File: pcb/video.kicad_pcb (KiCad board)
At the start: 4 copper layers, 159.9 x 99.9 mm, 170 parts, among them J1 09031966921, J3 Conn_02x07_Counter_Clockwise, J7 DB15_Female_HighDensity, J8 HDMI_A, SW1 SW_Push, U1 NCP115, U10 NCA9306DPH, U11 S62LV256AL-45TLI, U12 XC9572XL-10VQG44C, U2 LP3853ESX-3.3/NOPB, U3 LCMXO2-1200HC-4TG100I, U4 LCMXO2-7000HC-4TG144C, U5 THS8136, U6 TFP410PAP, U7 ESD224DQA, U8 ESD224DQA, U9 PCA9540BDP, X1 ASV-xxxMHz

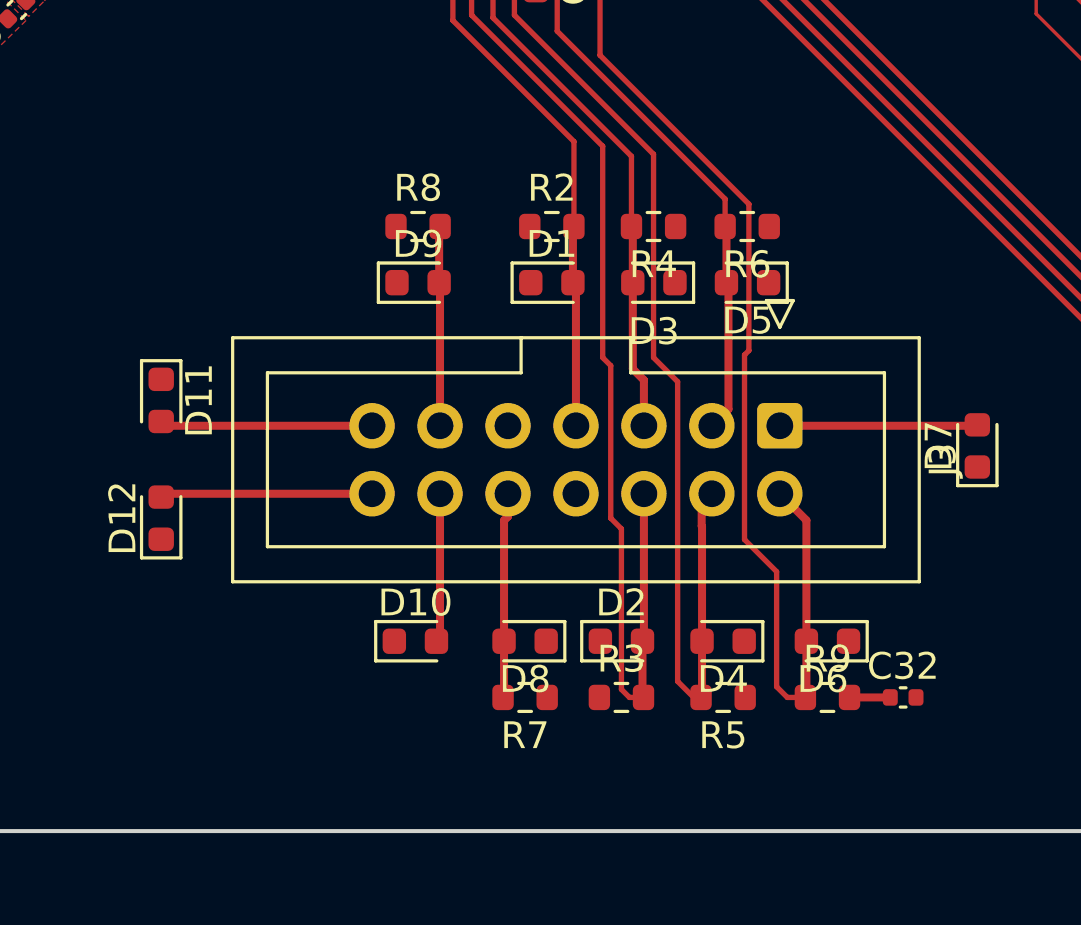
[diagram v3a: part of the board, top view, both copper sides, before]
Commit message: add the programming controller's jtag to the connector
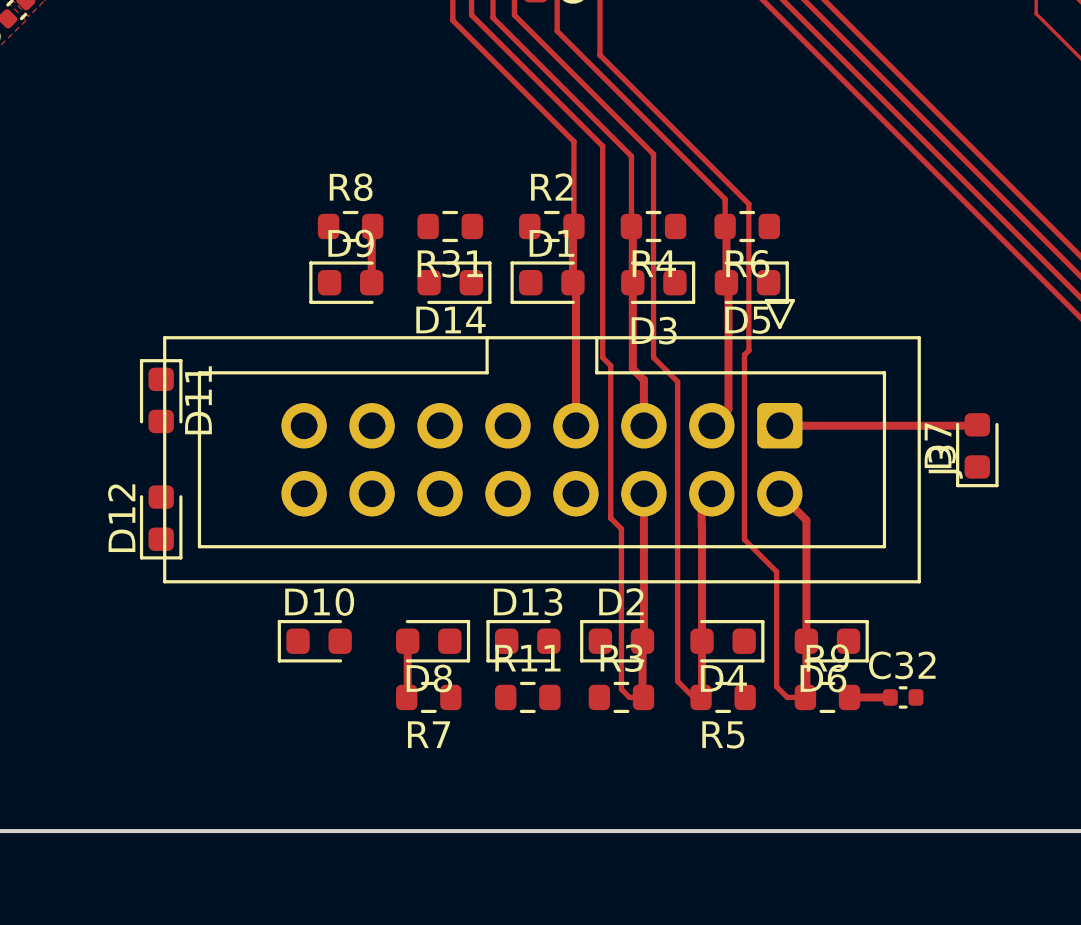
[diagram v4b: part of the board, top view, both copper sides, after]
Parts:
- added D13: D_TVS, Diode_SMD:D_0603_1608Metric, F.Cu at (152.7, 137.8)
- added D14: D_TVS, Diode_SMD:D_0603_1608Metric, F.Cu at (149.8, 124.4)
- added R11: 10k, Resistor_SMD:R_0603_1608Metric, F.Cu at (152.7, 139.9)
- added R31: 10k, Resistor_SMD:R_0603_1608Metric, F.Cu at (149.8, 122.3)
- J3: value Conn_02x07_Counter_Clockwise -> Conn_02x08_Counter_Clockwise; footprint Connector_IDC:IDC-Header_2x07_P2.54mm_Vertical -> Connector_IDC:IDC-Header_2x08_P2.54mm_Vertical
- moved D8 3.60 mm to (149.0, 137.8)
- moved R7 3.60 mm to (149.0, 139.9)
- moved D10 3.60 mm to (144.9, 137.8)
- moved D9 2.52 mm to (146.1, 124.4)
- moved R8 2.52 mm to (146.1, 122.3)
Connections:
- J3 pad 10: VIDEO_CTRL_CONFIG_SN -> GND
- J3 pad 11: BUS_CTRL_CONFIG_SN -> PROG_CTRL_TDO
- J3 pad 12: MISO -> VIDEO_CTRL_CONFIG_SN
- J3 pad 13: MOSI -> BUS_CTRL_CONFIG_SN
- J3 pad 14: CCK -> MISO
- J3 pad 8: GND -> PROG_CTRL_TDI
- U12 pad 10: (no net) -> JTAG_TMS_IN
- U12 pad 11: (no net) -> JTAG_TCK_IN
- U12 pad 24: (no net) -> PROG_CTRL_TDO
- U12 pad 9: (no net) -> PROG_CTRL_TDI
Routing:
- net CCK: track 7.93 -> 0.18 mm
- net MOSI: track 7.95 -> 0.23 mm
- net VIDEO_CTRL_CONFIG_SN: track 7.69 -> 2.12 mm
- net MISO: track 5.57 -> 0.19 mm
- net BUS_CTRL_CONFIG_SN: track 7.48 -> 2.16 mm

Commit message: add shield
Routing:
- net PROG_CTRL_TDI: track 0.00 -> 46.6 mm
- net PROG_CTRL_TDO: track 0.00 -> 41.2 mm, vias 0 -> 2
- net VIDEO_CTRL_CONFIG_SN: track 2.12 -> 28.0 mm
- net CONN_32: track 17.1 -> 0.00 mm
- net CONN_31: track 0.00 -> 17.1 mm
- net VGA_DDC_SCL: track 32.1 -> 19.4 mm
- net +5V: track 238.5 -> 230.5 mm
- net JTAG_TCK_IN: track 42.7 -> 50.4 mm
- net VGA_HSYNC: track 91.3 -> 84.6 mm
- net MISO: track 0.19 -> 6.19 mm
- net BUS_CTRL_CONFIG_SN: track 2.16 -> 7.51 mm
- net VGA_VSYNC: track 99.8 -> 94.5 mm
- net CCK: track 0.18 -> 5.39 mm
- net MOSI: track 0.23 -> 5.41 mm
- net JTAG_TMS_IN: track 27.8 -> 30.6 mm
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
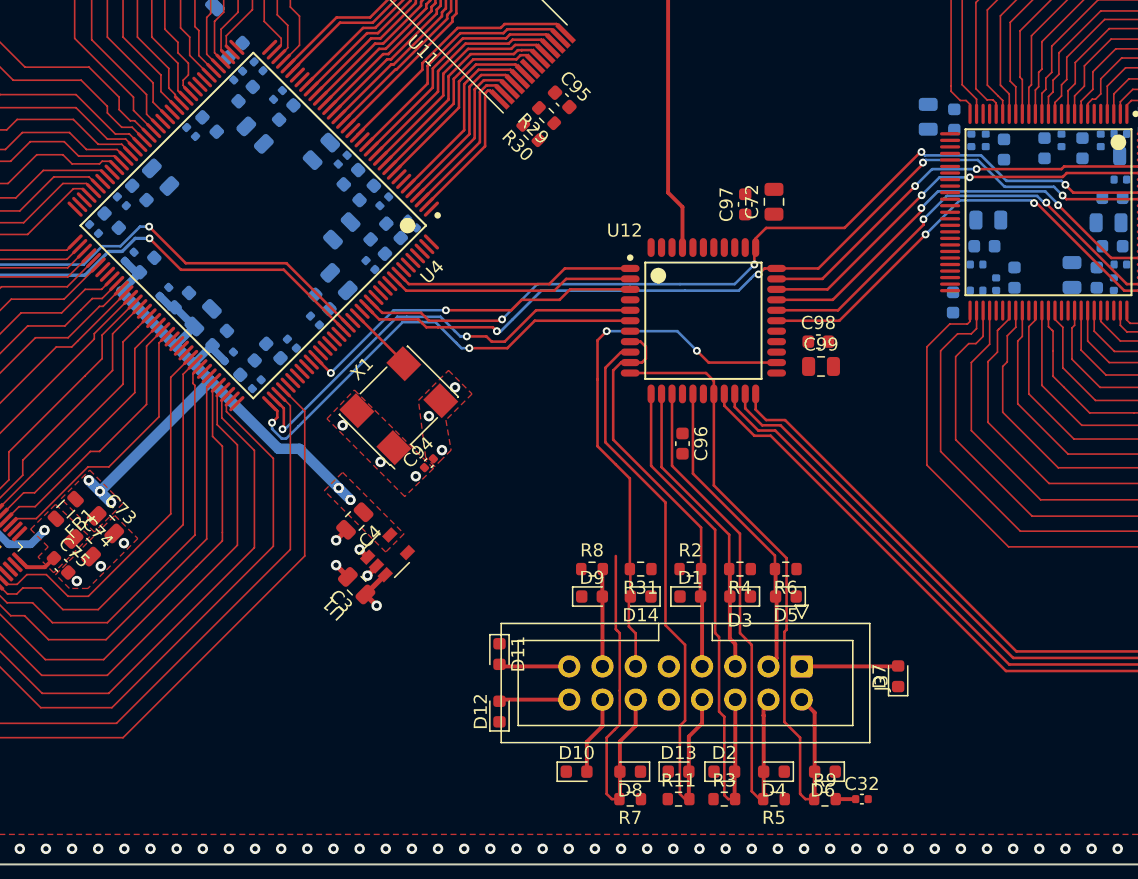
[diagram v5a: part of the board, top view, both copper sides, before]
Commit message: finish routing essential programming nets
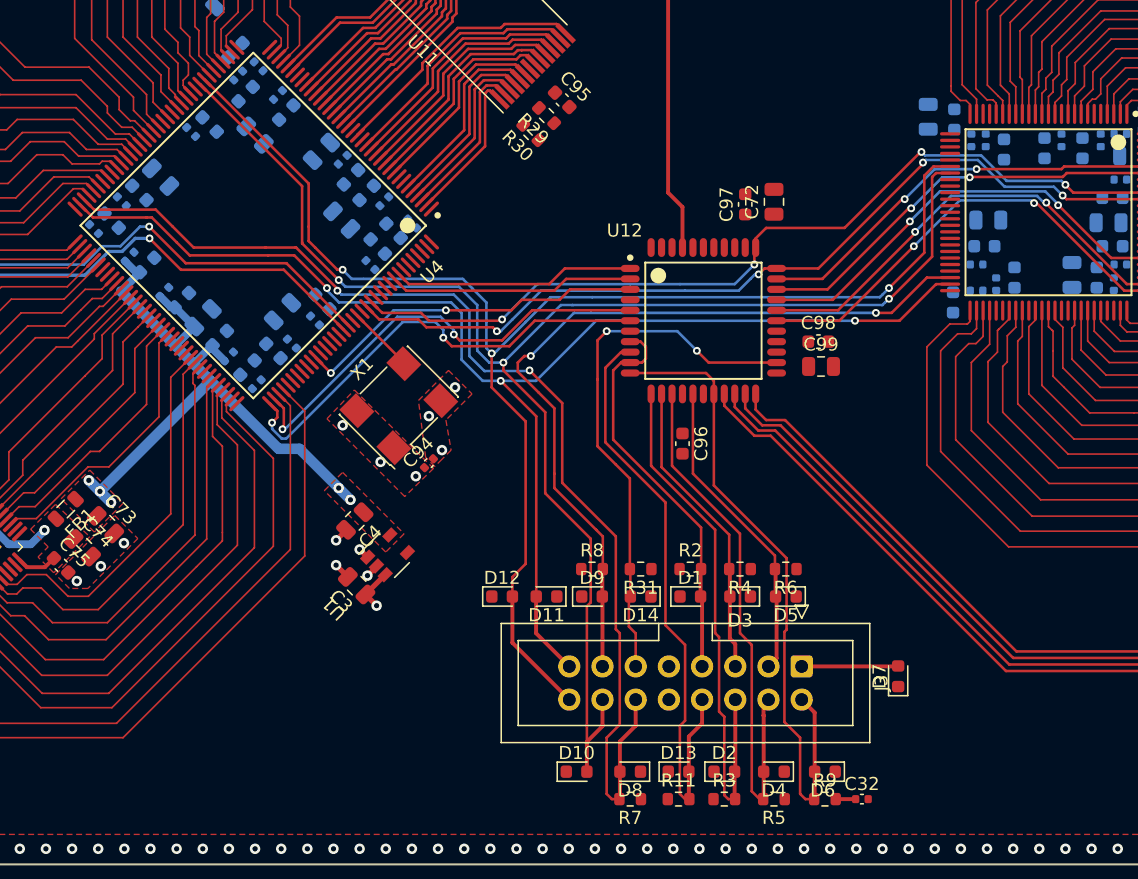
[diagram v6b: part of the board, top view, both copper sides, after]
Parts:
- moved D12 8.80 mm to (139.2, 124.4), turned to 0 degrees
- moved D11 5.69 mm to (142.6, 124.4), turned to 180 degrees
- moved C48 4.89 mm to (122.4, 102.6), turned to -135 degrees
- moved C69 0.82 mm to (126.9, 95.6), turned to 135 degrees
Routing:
- net MISO: track 6.19 -> 120.8 mm, vias 0 -> 3
- net CCK: track 5.39 -> 109.5 mm, vias 0 -> 3
- net MOSI: track 5.41 -> 101.5 mm, vias 0 -> 3
- net VIDEO_CTRL_CONFIG_SN: track 28.0 -> 86.6 mm, vias 0 -> 2
- net BUS_CTRL_CONFIG_SN: track 7.51 -> 61.8 mm, vias 0 -> 2
